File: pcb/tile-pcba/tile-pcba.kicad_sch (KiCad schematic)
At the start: 16 parts, among them IC1 THVD1420DR, J1 LED Strip, J2 UPDI, J5 12V, J6 RS-485 Jack, U1 ATtiny3224-X

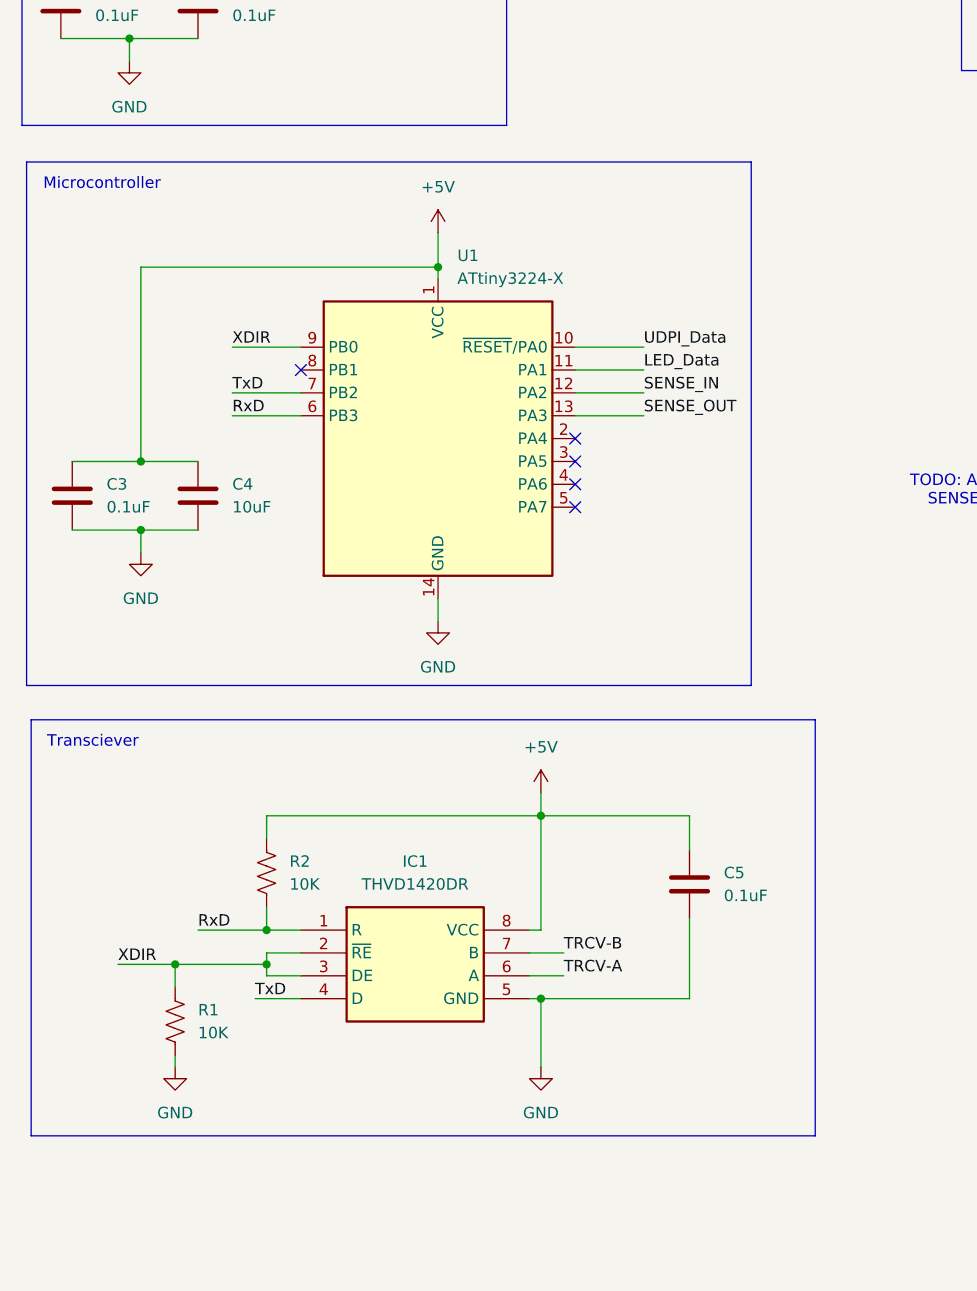
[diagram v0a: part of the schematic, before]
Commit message: Small changes the original tile, plus a pcba version with alternate parts that are available from JLCPCB.
Will likely collapse tile and tile-pcba once its confirmed tile-pcba is working
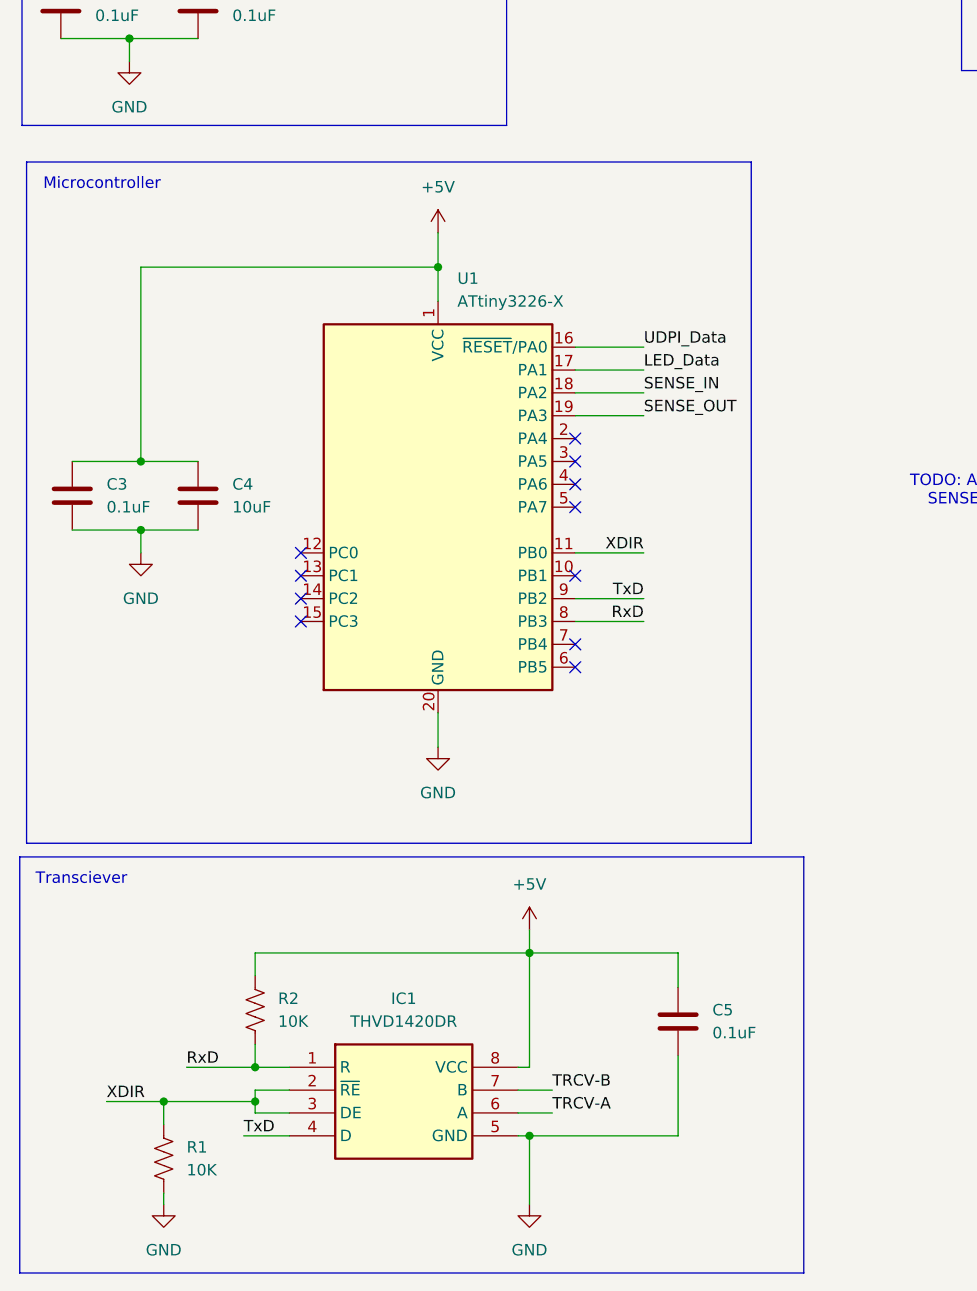
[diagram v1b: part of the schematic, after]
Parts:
- C1, C2, C3, C5: LCSC (none) -> C49678
- C4: LCSC (none) -> C1713
- C7: LCSC (none) -> C249915
- IC1: LCSC (none) -> C3235215
- J1: LCSC (none) -> C92159
- J5: LCSC (none) -> C158012
- PS1: LCSC (none) -> C2867465
- R1, R2: LCSC (none) -> C17414
- R3: LCSC (none) -> C17630
- U1: value ATtiny3224-X -> ATtiny3226-X; footprint Package_SO:TSSOP-14_4.4x5mm_P0.65mm -> Package_SO:SSOP-20_5.3x7.2mm_P0.65mm; symbol MCU_Microchip_ATtiny:ATtiny3224-X -> MCU_Microchip_ATtiny:ATtiny3226-X; LCSC (none) -> C3235640; Manufacturer Part Number ATTINY3224-XF -> ATTINY3226-XF; Mouser Part Number 579-ATTINY3224-XF -> 579-ATTINY3226-XF; Mouser Price/Stock https://www.mouser.com/en/ProductDetail/579-ATTINY3224-XF -> https://www.mouser.com/en/ProductDetail/Microchip-Technolog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
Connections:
- net GND: now also U1.20 (GND); no longer U1.14 (GND)
- net LED_Data: now also U1.17 (PA1); no longer U1.11 (PA1)
- net RxD: now also U1.8 (PB3); no longer U1.6 (PB3)
- net SENSE_IN: now also U1.18 (PA2); no longer U1.12 (PA2)
- net SENSE_OUT: now also U1.19 (PA3); no longer U1.13 (PA3)
- net TxD: now also U1.9 (PB2); no longer U1.7 (PB2)
- net UDPI_Data: now also U1.16 (~{RESET}/PA0); no longer U1.10 (~{RESET}/PA0)
- net XDIR: now also U1.11 (PB0); no longer U1.9 (PB0)
- no-connect marks 5 -> 11
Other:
- moved on the sheet: C5, IC1, R1, R2
